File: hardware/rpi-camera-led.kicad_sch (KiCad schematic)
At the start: 20 parts, among them J1 FFC 15P 1.0mm (to Raspberry P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, J2 FFC 15P 1.0mm (to camera), J3 Qwiic (JST SH 1.0mm), J4 SWD program header 2.54mm, Q1 AO3400A, Q2 Phototransistor, U1 CH32V003A4M6

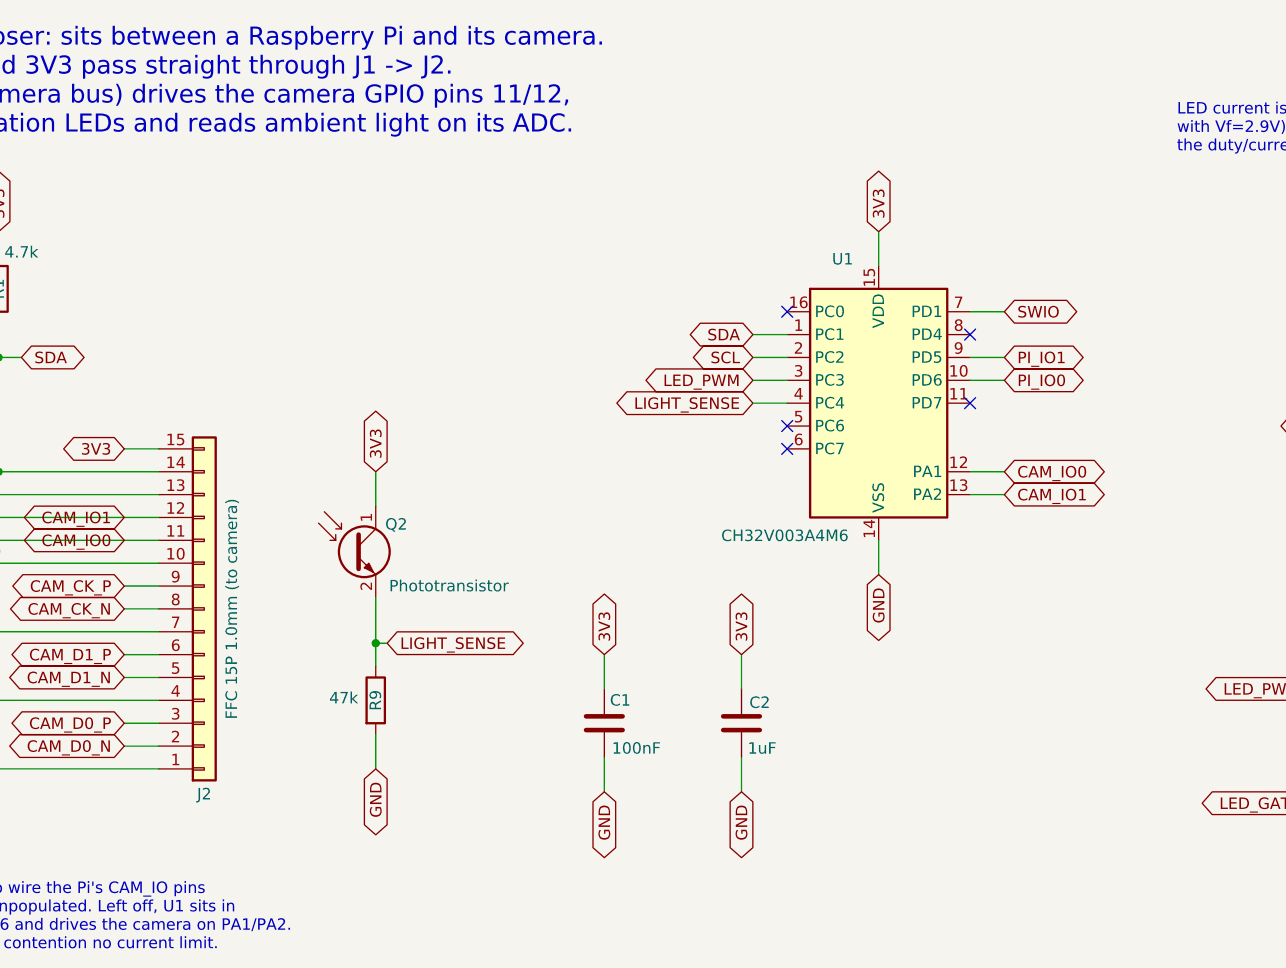
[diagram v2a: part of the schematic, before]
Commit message: Tim's KiCad session: U1 pins rearranged, bus routing extended
Committing work in progress so it is not lost.  U1's assignment moves
toward the arrangement Tim asked about -- camera GPIOs on pins 7/8, Pi
sense on 9/10, I2C also brought out to 5/6 and 11/12 -- J2 goes back to
the reversed pin mapping, and the board grows to 37 track segments with
unconnected down from 49 to 35.

It does not pass its checks yet.  Recorded here rather than fixed,
because each of these is a design decision:

  * ERC error, U1.13 (PA2) is connected to nothing, with a 0.038mm wire
    fragment left behind at the same point -- the remains of dragging
    CAM_IO1 off that pin.
  * SWIO and CAM_IO1 are the same net.  U1.7 is PD1, the single-wire
    debug pin, and J4.2 sits on it, so KiCad merges the two and keeps
    CAM_IO1.  Programming the part would drive the camera's GPIO1 and
    the camera would fight the debugger.
  * SCL is wired to U1.11 and SDA to U1.12, which are PD7 and PA1.
    Neither can be I2C on this package -- the peripheral only reaches
    PC1/PC2 (pins 1/2), since both AFIO remaps need PD0 or PC5 and the
    SOP-16 bonds out neither.  PD7 is worse than useless here: it is
    NRST until the RST_MODE option byte says otherwise, so a factory
    part would sit in reset for every low half-cycle of SCL.  SDA on
    U1.5 and SCL on U1.6 (PC6/PC7) are inert rather than harmful.
  * Four no-connect flags now dangle where pins used to be.

The board matches the schematic (parity 0), so the same joins exist in
copper: 116 DRC violations.

Co-Authored-By: Claude Opus 5 (1M context) <noreply@anthropic.com>
Claude-Session: https://claude.ai/code/session_01E6VQHygrbAGSqdngQQsBdx
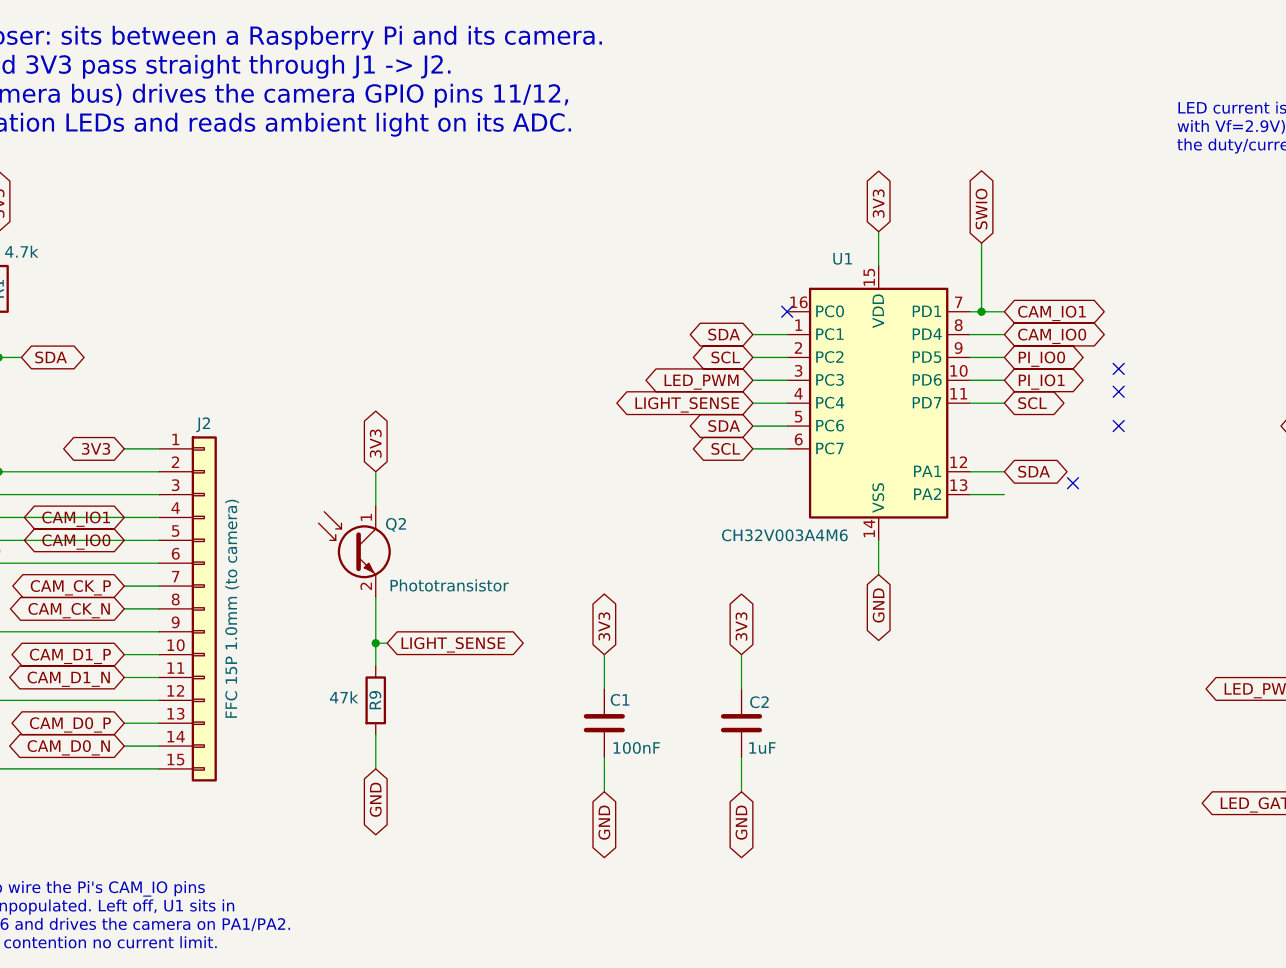
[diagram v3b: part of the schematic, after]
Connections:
- net SWIO is gone; now on net CAM_IO1: J4.2 (Pin_2), U1.7 (PD1)
- net 3V3: now also J2.1 (Pin_1); no longer J2.15 (Pin_15)
- net CAM_CK_P: now also J2.7 (Pin_7); no longer J2.9 (Pin_9)
- net CAM_D0_N: now also J2.14 (Pin_14); no longer J2.2 (Pin_2)
- net CAM_D0_P: now also J2.13 (Pin_13); no longer J2.3 (Pin_3)
- net CAM_D1_N: now also J2.11 (Pin_11); no longer J2.5 (Pin_5)
- net CAM_D1_P: now also J2.10 (Pin_10); no longer J2.6 (Pin_6)
- net CAM_IO0: now also J2.5 (Pin_5), U1.8 (PD4); no longer J2.11 (Pin_11), U1.12 (PA1)
- net CAM_IO1: now also J2.4 (Pin_4); no longer J2.12 (Pin_12), U1.13 (PA2)
- net GND: now also J2.12 (Pin_12), J2.15 (Pin_15), J2.6 (Pin_6), J2.9 (Pin_9); no longer J2.1 (Pin_1), J2.10 (Pin_10), J2.4 (Pin_4), J2.7 (Pin_7)
- net PI_IO0: now also U1.9 (PD5); no longer U1.10 (PD6)
- net PI_IO1: now also U1.10 (PD6); no longer U1.9 (PD5)
- net SCL: now also J2.3 (Pin_3), U1.11 (PD7), U1.6 (PC7); no longer J2.13 (Pin_13)
- net SDA: now also J2.2 (Pin_2), U1.12 (PA1), U1.5 (PC6); no longer J2.14 (Pin_14)
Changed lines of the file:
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@@
 	)
 	(junction
+		(at 161.29 49.53)
+		(diameter 0)
+		(color 0 0 0 0)
+	)
+	(junction
 		(at 220.98 81.28)
 		(diameter 0)
@@
 	)
 	(no_connect
-		(at 139.7 64.77)
+		(at 171.45 68.58)
 	)
 	(no_connect
@@
 	)
 	(no_connect
-		(at 139.7 62.23)
+		(at 176.53 62.23)
 	)
 	(no_connect
-		(at 160.02 52.07)
+		(at 176.53 55.88)
 	)
 	(no_connect
-		(at 160.02 59.69)
+		(at 176.53 58.42)
 	)
 	(wire
@@
 	(wire
 		(pts
-			(xy 160.02 57.15) (xy 163.83 57.15)
+			(xy 160.02 52.07) (xy 163.83 52.07)
 		)
 		(stroke
@@
 	(wire
 		(pts
+			(xy 160.02 57.15) (xy 163.83 57.15)
+		)
+		(stroke
+			(width 0)
+			(type default)
+		)
+	)
+	(wire
+		(pts
 			(xy 44.45 54.61) (xy 46.99 54.61)
 		)
@@
 	(wire
 		(pts
+			(xy 135.89 62.23) (xy 139.7 62.23)
+		)
+		(stroke
+			(width 0)
+			(type default)
+		)
+	)
+	(wire
+		(pts
+			(xy 135.89 64.77) (xy 139.7 64.77)
+		)
+		(stroke
+			(width 0)
+			(type default)
+		)
+	)
+	(wire
+		(pts
 			(xy 27.94 90.17) (xy 31.75 90.17)
 		)
@@
 	(wire
 		(pts
-			(xy 160.02 49.53) (xy 163.83 49.53)
+			(xy 160.02 49.53) (xy 161.29 49.53)
 		)
 		(stroke
@@
 	(wire
 		(pts
+			(xy 161.29 49.53) (xy 163.83 49.53)
+		)
+		(stroke
+			(width 0)
+			(type default)
+		)
+	)
+	(wire
+		(pts
 			(xy 200.66 104.14) (xy 200.66 105.41)
 		)
@@
 	(wire
 		(pts
+			(xy 161.29 41.91) (xy 161.29 49.53)
+		)
+		(stroke
+			(width 0)
+			(type default)
+		)
+	)
+	(wire
+		(pts
 			(xy 212.09 81.28) (xy 212.09 99.06)
 		)
@@
 	(wire
 		(pts
+			(xy 160.02 59.69) (xy 163.83 59.69)
+		)
+		(stroke
+			(width 0)
+			(type default)
+		)
+	)
+	(wire
+		(pts
 			(xy 212.09 81.28) (xy 220.98 81.28)
 		)
@@
 		)
 	)
+	(global_label "SDA"
+		(shape bidirectional)
+		(at 163.83 67.31 0)
+		(fields_autoplaced yes)
+		(effects
+			(font
+				(size 1.27 1.27)
+			)
+			(justify left)
+		)
+		(property "Intersheetrefs" "${INTERSHEET_REFS}"
+			(at 171.4946 67.31 0)
+			(effects
+				(font
+					(size 1.27 1.27)
+				)
+				(justify left)
+				(hide yes)
+			)
+		)
+	)
 	(global_label "3V3"
 		(shape bidirectional)
@@
 		)
 	)
+	(global_label "SCL"
+		(shape bidirectional)
+		(at 135.89 64.77 180)
+		(fields_autoplaced yes)
+		(effects
+			(font
+				(size 1.27 1.27)
+			)
+			(justify right)
+		)
+		(property "Intersheetrefs" "${INTERSHEET_REFS}"
+			(at 135.89 64.77 0)
+			(effects
+				(font
+					(size 1.27 1.27)
+				)
+				(hide yes)
+			)
+		)
+	)
 	(global_label "PI_IO0"
 		(shape bidirectional)
-		(at 163.83 57.15 0)
+		(at 163.83 54.61 0)
 		(fields_autoplaced yes)
 		(effects
@@
 		)
 		(property "Intersheetrefs" "${INTERSHEET_REFS}"
-			(at 173.9137 57.15 0)
+			(at 173.9137 54.61 0)
 			(effects
 				(font
@@
 		)
 	)
+	(global_label "SDA"
+		(shape bidirectional)
+		(at 135.89 62.23 180)
+		(fields_autoplaced yes)
+		(effects
+			(font
+				(size 1.27 1.27)
+			)
+			(justify right)
+		)
+		(property "Intersheetrefs" "${INTERSHEET_REFS}"
+			(at 135.89 62.23 0)
+			(effects
+				(font
+					(size 1.27 1.27)
+				)
+				(hide yes)
+			)
+		)
+	)
+	(global_label "SCL"
+		(shape bidirectional)
+		(at 163.83 59.69 0)
+		(fields_autoplaced yes)
+		(effects
+			(font
+				(size 1.27 1.27)
+			)
+			(justify left)
+		)
+		(property "Intersheetrefs" "${INTERSHEET_REFS}"
+			(at 171.4341 59.69 0)
+			(effects
+				(font
+					(size 1.27 1.27)
+				)
+				(justify left)
+				(hide yes)
+			)
+		)
+	)
 	(global_label "CAM_D0_N"
 		(shape bidirectional)
@@
 	(global_label "PI_IO1"
 		(shape bidirectional)
-		(at 163.83 54.61 0)
+		(at 163.83 57.15 0)
 		(fields_autoplaced yes)
 		(effects
@@
 		)
 		(property "Intersheetrefs" "${INTERSHEET_REFS}"
-			(at 173.9137 54.61 0)
+			(at 173.9137 57.15 0)
 			(effects
 				(font
@@
 	(global_label "SWIO"
 		(shape bidirectional)
-		(at 163.83 49.53 0)
+		(at 161.29 41.91 90)
 		(fields_autoplaced yes)
 		(effects
@@
 		)
 		(property "Intersheetrefs" "${INTERSHEET_REFS}"
-			(at 163.83 49.53 0)
+			(at 161.29 33.2173 90)
 			(effects
 				(font
 					(size 1.27 1.27)
 				)
+				(justify left)
 				(hide yes)
 			)
@@
 	(global_label "CAM_IO0"
 		(shape bidirectional)
-		(at 163.83 67.31 0)
+		(at 163.83 52.07 0)
 		(fields_autoplaced yes)
 		(effects
@@
 		)
 		(property "Intersheetrefs" "${INTERSHEET_REFS}"
-			(at 163.83 67.31 0)
+			(at 163.83 52.07 0)
 			(effects
 				(font
@@
 	(global_label "CAM_IO1"
 		(shape bidirectional)
-		(at 163.83 69.85 0)
+		(at 163.83 49.53 0)
 		(fields_autoplaced yes)
 		(effects
@@
 		)
 		(property "Intersheetrefs" "${INTERSHEET_REFS}"
-			(at 163.83 69.85 0)
+			(at 163.83 49.53 0)
 			(effects
 				(font
@@
 		(lib_id "Connector_Generic:Conn_01x15")
 		(at 74.93 82.55 0)
-		(mirror x)
 		(unit 1)
 		(exclude_from_sim no)
@@
 		(dnp no)
 		(property "Reference" "J2"
-			(at 74.93 103.124 0)
+			(at 74.93 61.976 0)
 			(effects
 				(font

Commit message: J2 becomes the top-contact part, so both cables are standard
With J1 and J2 both bottom-contact, the camera-side cable segment had to
be a same-side (type 1) FFC -- not a part you can buy as a Raspberry Pi
camera cable.  Making J2 top-contact means the interposer flips which
face of the cable carries copper, and both segments become ordinary
opposite-side Raspberry Pi camera cables.

The reasoning, since it is easy to get backwards:

  - the Raspberry Pi's CSI socket is top-contact (SFW15R-2STE1LF) and
    the camera module's is bottom-contact (per Gert van Loo, who
    designed the camera board), which is exactly why the standard cable
    is opposite-side -- "type 2" in JUSHUO's and Gert's numbering;
  - cutting one continuous cable anywhere yields one same-side half and
    one opposite-side half, so an interposer whose two connectors want
    copper on the SAME face forces one odd cable, and one that wants it
    on OPPOSITE faces takes two standard cables;
  - F.Cu + bottom contact wants copper down, F.Cu + top contact wants
    copper up.  J1 bottom / J2 top is therefore the pairing that works.

Nothing moves.  The two variants share a land pattern (verified against
both JUSHUO drawings in fd472db), so this is metadata only: pad 1 is
still at 26.200,24.931 on J1 and 38.800,38.931 on J2, alignment is still
0.000000mm, both pad columns are still 6.3000mm off centre, and DRC
still reports 0 schematic-parity issues.  The existing routing and the
reversed J1.k <-> J2.(16-k) netlist stay valid -- that mapping connects
the pads that physically face each other, which is both the straight
route and the electrically transparent one.

Contact side is now stated everywhere it can be misread: in each
symbol's Value, in the MPN (with LCSC codes and the Amphenol
equivalents, which differ between the two), and as a BOTTOM CONTACT /
TOP CONTACT marker on F.Fab.

check_schematic.py still fails, unchanged and for unrelated reasons:
its EXPECTED table still describes the old pin-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
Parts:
- J1: value FFC 15P 1.0mm (to Raspberry Pi) -> FFC 15P 1.0mm bottom contact (to Raspberry Pi); MPN JUSHUO AFA07-S15FCA-00 / Amphenol SFW15R-1STE1LF -> JUSHUO AFA07-S15FCA-00 (LCSC C262721) / Amphenol SFW15R-1ST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
- J2: value FFC 15P 1.0mm (to camera) -> FFC 15P 1.0mm top contact (to camera); footprint Connector_FFC-FPC:JUSHUO_AFA07-S15FCA-00_1x15-1MP_P1.0mm_Horizontal -> rpi-camera-led:JUSHUO_AFA07-S15ECA-00_1x15-1MP_P1.0mm_Horizontal; MPN JUSHUO AFA07-S15FCA-00 / Amphenol SFW15R-1STE1LF -> JUSHUO AFA07-S15ECA-00 (LCSC C262742) / Amphenol SFW15R-2ST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
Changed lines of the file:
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@@
 			)
 		)
-		(property "Value" "FFC 15P 1.0mm (to camera)"
+		(property "Value" "FFC 15P 1.0mm top contact (to camera)"
 			(at 77.978 82.55 90)
 			(effects
@@
 			)
 		)
-		(property "Footprint" "Connector_FFC-FPC:JUSHUO_AFA07-S15FCA-00_1x15-1MP_P1.0mm_Horizontal"
+		(property "Footprint" "rpi-camera-led:JUSHUO_AFA07-S15ECA-00_1x15-1MP_P1.0mm_Horizontal"
 			(at 74.93 82.55 0)
 			(effects
@@
 			)
 		)
-		(property "MPN" "JUSHUO AFA07-S15FCA-00 / Amphenol SFW15R-1STE1LF"
+		(property "MPN" "JUSHUO AFA07-S15ECA-00 (LCSC C262742) / Amphenol SFW15R-2STE1LF"
 			(at 74.93 82.55 0)
 			(effects
@@
 			)
 		)
-		(property "Value" "FFC 15P 1.0mm (to Raspberry Pi)"
+		(property "Value" "FFC 15P 1.0mm bottom contact (to Raspberry Pi)"
 			(at 20.066 82.55 90)
 			(effects
@@
 			)
 		)
-		(property "MPN" "JUSHUO AFA07-S15FCA-00 / Amphenol SFW15R-1STE1LF"
-			(at 22.86 82.55 0)
-			(effects
+		(property "MPN" "JUSHUO AFA07-S15FCA-00 (LCSC C262721) / Amphenol SFW15R-1STE1LF"
+			(at 22.86 82.55 0)
+			(effects

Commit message: Build 3D models for the FFC connectors, and wire both up
KiCad's stock footprint points at
Connector_FFC-FPC.3dshapes/JUSHUO_AFA07-S15FCA-00_...step, which does not
exist.  Not in the snap, and not upstream either: kicad-packages3D ships
112 files in that library and none of them are JUSHUO.  Component Search
Engine has one, but SamacSys's terms do not permit redistribution, so it
cannot go in an Apache-2.0 repository.

So gen_connector_model.py builds one from the manufacturer's drawing,
which we can carry.  Everything dimensioned comes from that drawing or
from KiCad's stock footprint, whose F.Fab outline is the body outline and
whose land pattern was already verified against the drawing pad for pad:
the plan outline from F.Fab, 2.50mm height from the side view and the
"H2.5" in the product name, contact tails on the land pattern itself, and
the colours from note 1 ("Housing: ... Color: natural", "Latch: ...
Color: black").  The envelope comes out 22.00 x 6.95 x 2.50 mm, which is
DIM D, the F.Fab depth and that 2.50 respectively.  The cable slot is the
one invented feature -- the drawing does not dimension it -- and it cuts
only into the front face, so the outside envelope stays exact.

Both STEP and WRL are written.  The WRL scale is not obvious and is easy
to get wrong, so it was measured rather than assumed: a known-good
library model has a WRL Z span of 0.7864 against a STEP Z span of exactly
2.0000, which is the 2.54 factor, and WRL Y is the negation of footprint
Y.

J1 was still on the stock footprint, so it now gets a project copy too --
otherwise half the board would keep referencing a model that isn't there.
Both connectors are now project-local, footprint and model.

What the models immediately show is that both connectors are turned the
wrong way round.  Their housings are flush with the board edges (J1 ends
at x=20.000, J2 at x=45.000, outline 20.0-45.0), which points both mouths
inward, 14.4mm apart, facing each other across the middle of the board.
T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
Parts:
- J1: footprint Connector_FFC-FPC:JUSHUO_AFA07-S15FCA-00_1x15-1MP_P1.0mm_Horizontal -> rpi-camera-led:JUSHUO_AFA07-S15FCA-00_1x15-1MP_P1.0mm_Horizontal
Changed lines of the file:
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@@
 			)
 		)
-		(property "Footprint" "Connector_FFC-FPC:JUSHUO_AFA07-S15FCA-00_1x15-1MP_P1.0mm_Horizontal"
+		(property "Footprint" "rpi-camera-led:JUSHUO_AFA07-S15FCA-00_1x15-1MP_P1.0mm_Horizontal"
 			(at 22.86 82.55 0)
 			(effects
